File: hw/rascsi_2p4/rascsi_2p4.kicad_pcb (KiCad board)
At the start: 2 copper layers, 65 x 56 mm, 128 parts, among them J1 Raspberry_Pi_2_3, J10 Conn_01x04_Male, J2 DNP, J20 171826-4, J3 Conn_02x25_Odd_Even, J4 I2C Pinout, J5 DNP, J6 CONNFLY DB-25, J7 DNP, J8 USB_B_Micro, J9 Conn_02x25_Odd_Even, U1 74ALVC164245DGG, U2 74ALVC164245DGG, X1 Mac, X2 Dogcow, X3 Mac, X4 Dogcow, X5 Dogcow, X6 Dogcow, X7 Pi, X8 Pi

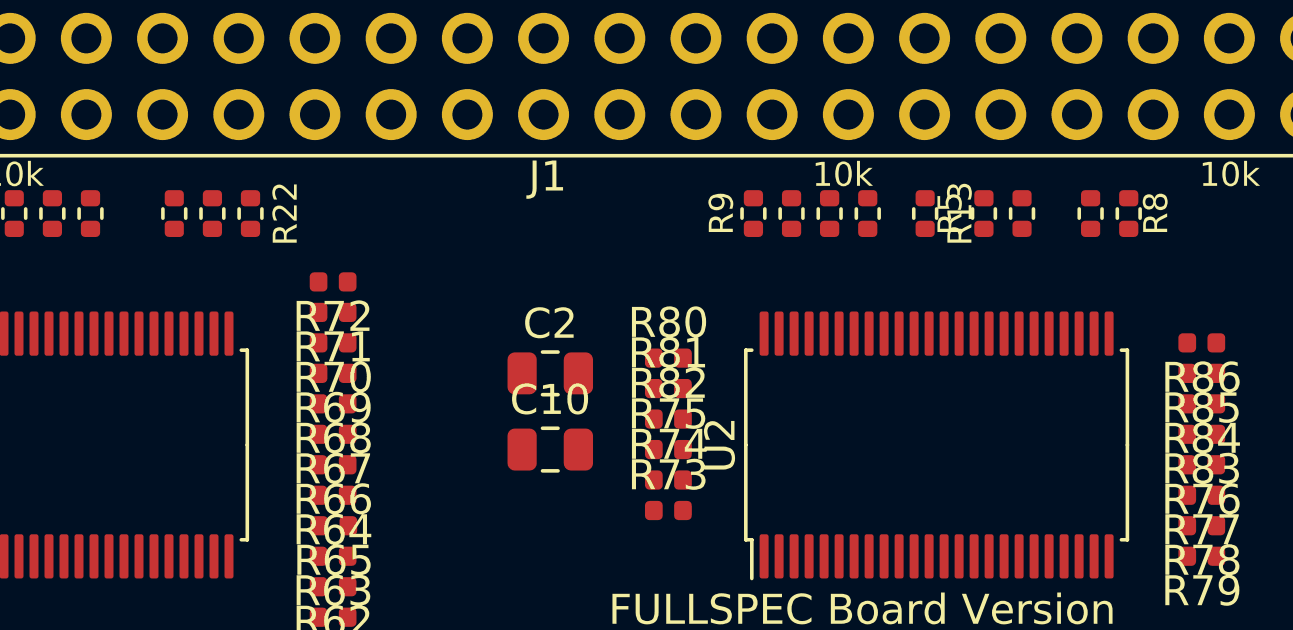
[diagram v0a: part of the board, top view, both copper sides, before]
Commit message: added intermediate routing results with 136 vias
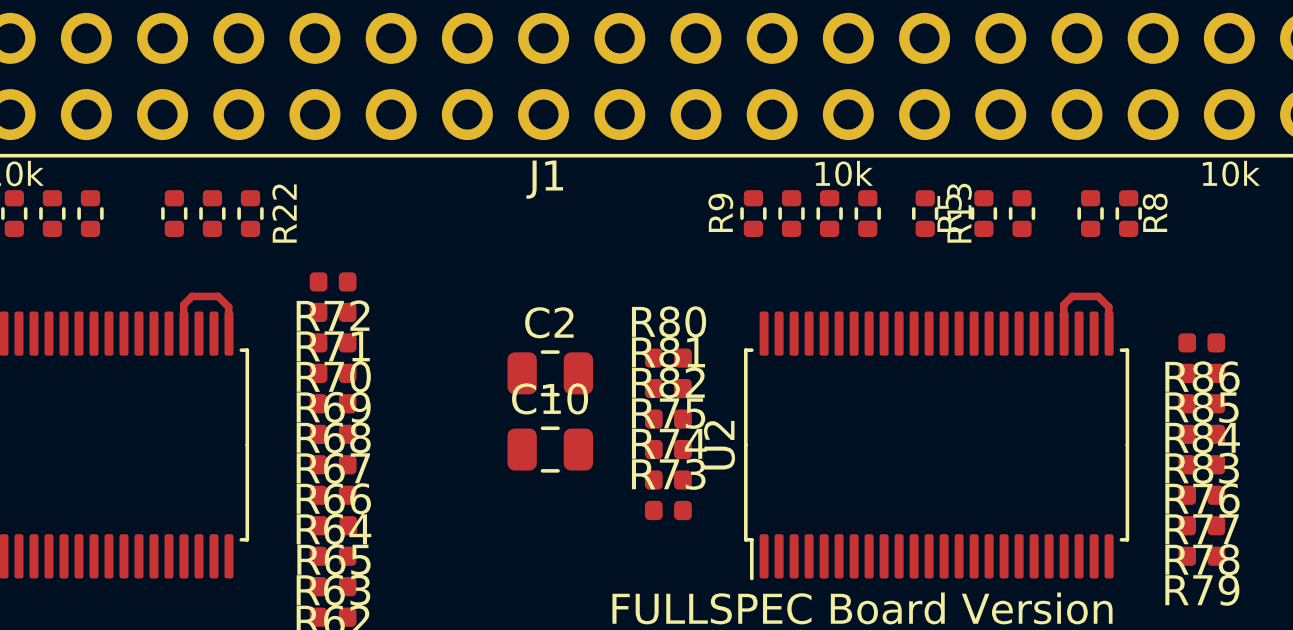
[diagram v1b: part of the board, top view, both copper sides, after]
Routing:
- net GND: track 0.00 -> 7.18 mm

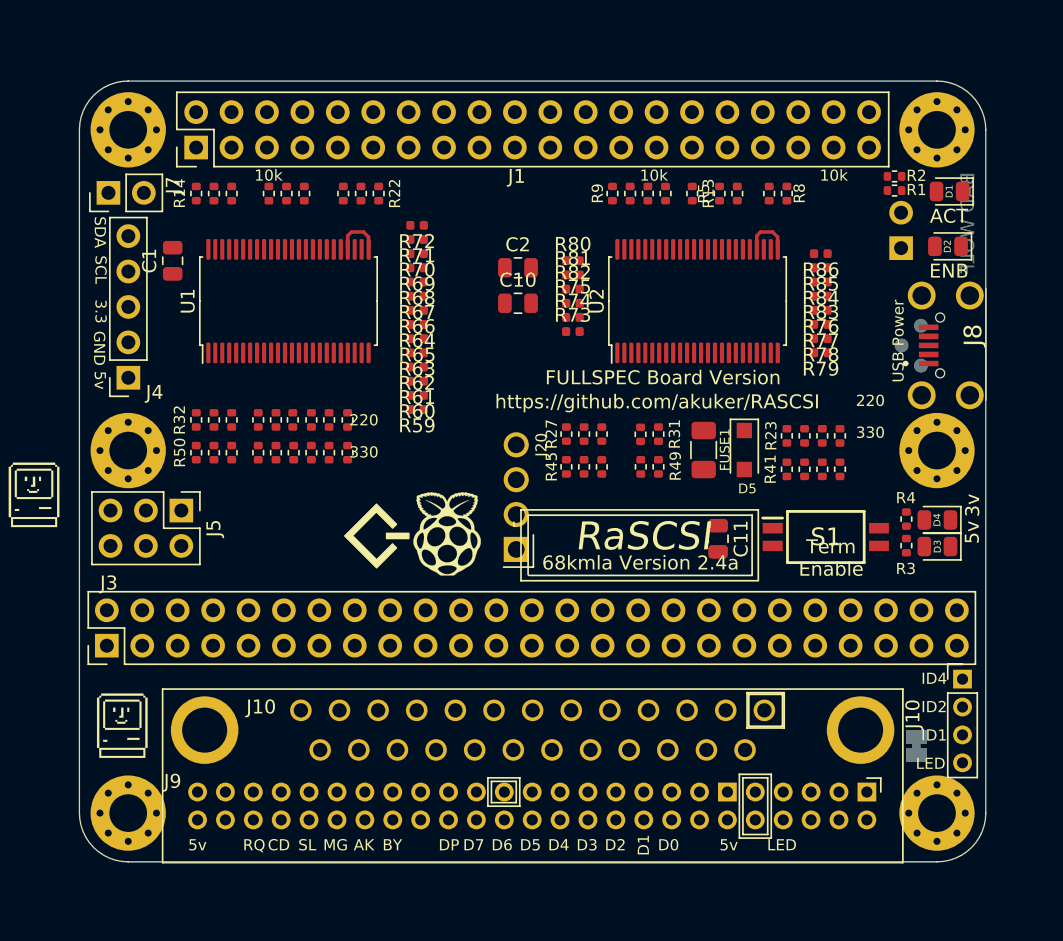
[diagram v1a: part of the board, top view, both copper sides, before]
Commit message: imported routed traces; fixed orientation of U1 and U2
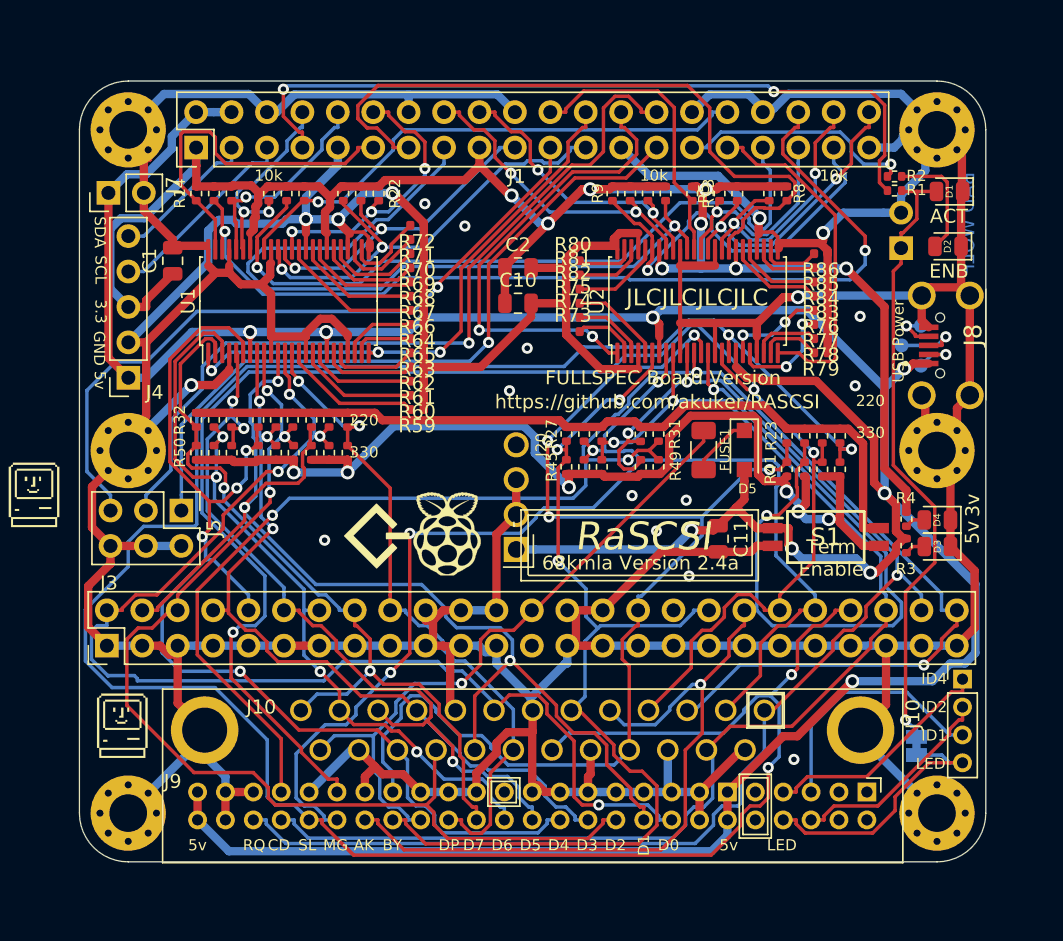
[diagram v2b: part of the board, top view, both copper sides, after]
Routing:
- net GND: track 7.18 -> 614.4 mm, vias 0 -> 19
- net +5V: track 0.00 -> 239.1 mm, vias 0 -> 9
- net C-SEL: track 0.00 -> 174.4 mm, vias 0 -> 4
- net +3V3: track 0.00 -> 133.7 mm, vias 0 -> 8
- net C-I_O: track 0.00 -> 119.3 mm, vias 0 -> 4
- net C-RST: track 0.00 -> 117.8 mm, vias 0 -> 3
- net C-ACK: track 0.00 -> 101.4 mm, vias 0 -> 3
- net C-REQ: track 0.00 -> 97.6 mm, vias 0 -> 3
- net C-MSG: track 0.00 -> 92.8 mm, vias 0 -> 4
- net C-C_D: track 0.00 -> 89.6 mm, vias 0 -> 2
- net C-ATN: track 0.00 -> 86.6 mm, vias 0 -> 4
- net C-D0: track 0.00 -> 86.0 mm, vias 0 -> 4
- net C-D1: track 0.00 -> 82.6 mm, vias 0 -> 3
- net C-D4: track 0.00 -> 80.6 mm, vias 0 -> 4
- net C-D2: track 0.00 -> 78.6 mm, vias 0 -> 3
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
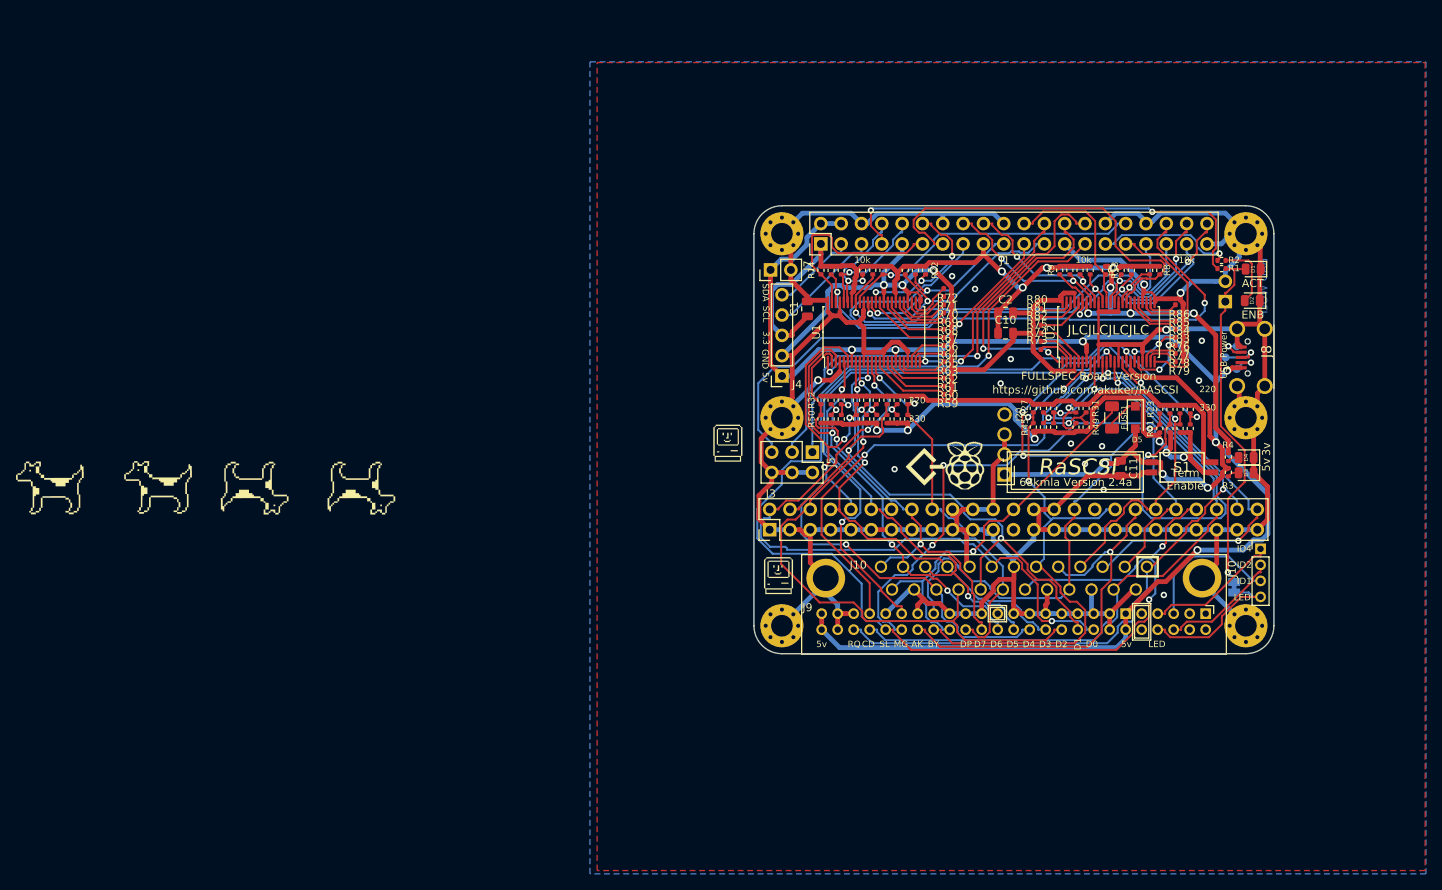
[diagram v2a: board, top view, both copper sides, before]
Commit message: added U1/U2 caps for 3.3V
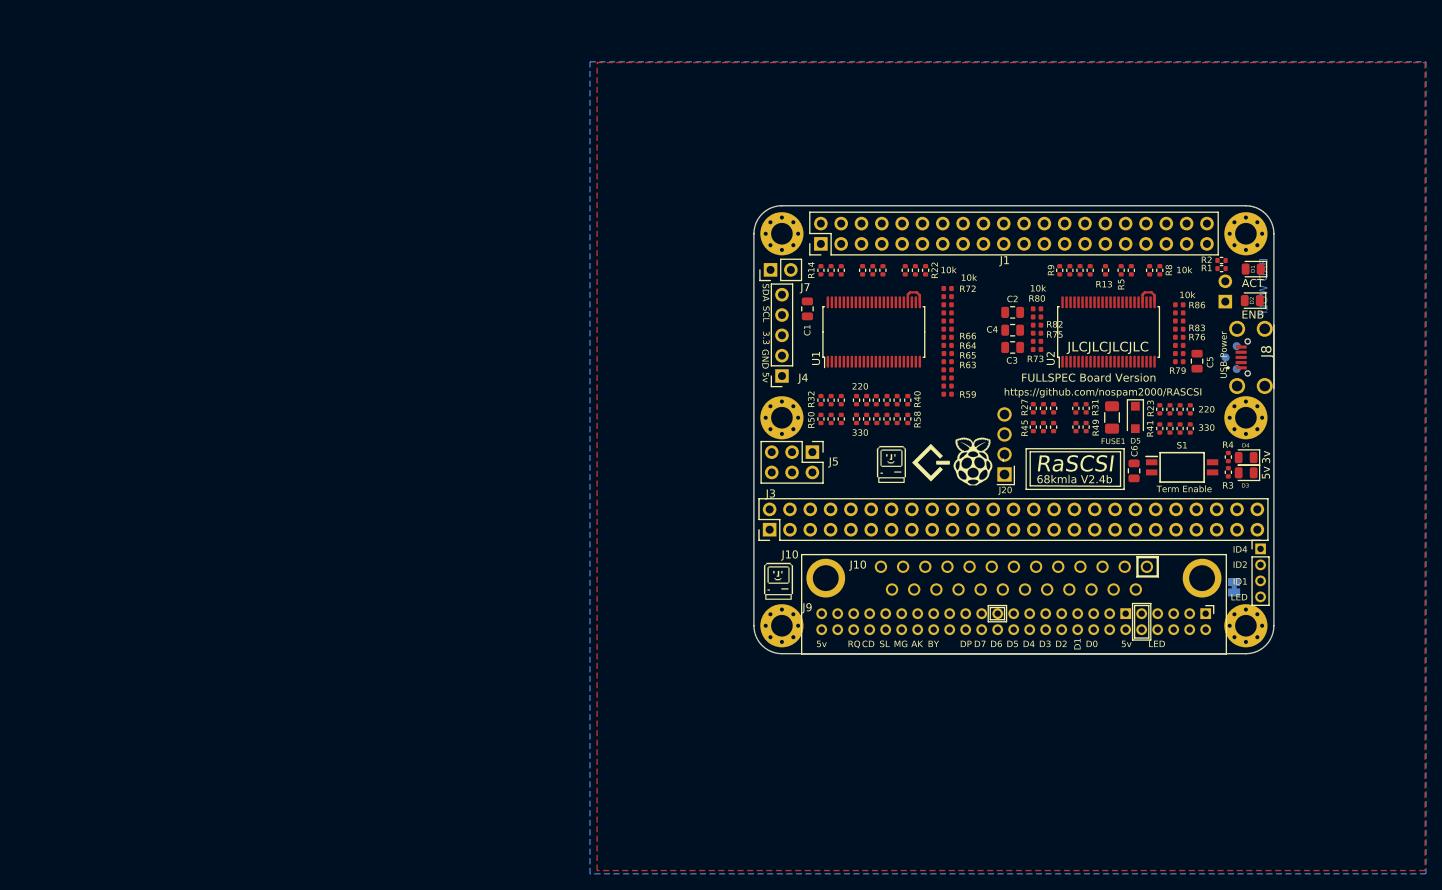
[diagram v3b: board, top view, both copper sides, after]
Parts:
- removed C11: 10u, Capacitor_SMD:C_0805_2012Metric
- removed X2, X4, X5, X6: Dogcow, SamacSys_Parts:dogcow
- added C4: 330n, Capacitor_SMD:C_0805_2012Metric, F.Cu at (206.8, 60.2)
- added C5: 330n, Capacitor_SMD:C_0805_2012Metric, F.Cu at (229.9, 61.9)
- added C6: 10u, Capacitor_SMD:C_0805_2012Metric, F.Cu at (222.0, 75.6)
- moved X3 20.6 mm to (191.7, 74.8)
- moved X7 1.14 mm to (201.9, 74.5)
- moved C3 0.97 mm to (206.8, 58.1)
- moved X8 0.96 mm to (196.5, 74.6)
- moved C2 0.89 mm to (206.8, 55.8)
- moved X1 0.71 mm to (177.6, 89.4)
- renumbered C10 to C3
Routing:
- net GND: track 614.4 -> 7.16 mm, vias 19 -> 0
- net +5V: track 239.1 -> 0.00 mm, vias 9 -> 0
- net C-SEL: track 174.4 -> 0.00 mm, vias 4 -> 0
- net +3V3: track 133.7 -> 0.00 mm, vias 8 -> 0
- net C-I_O: track 119.3 -> 0.00 mm, vias 4 -> 0
- net C-RST: track 117.8 -> 0.00 mm, vias 3 -> 0
- net C-ACK: track 101.4 -> 0.00 mm, vias 3 -> 0
- net C-REQ: track 97.6 -> 0.00 mm, vias 3 -> 0
- net C-MSG: track 92.8 -> 0.00 mm, vias 4 -> 0
- net C-C_D: track 89.6 -> 0.00 mm, vias 2 -> 0
- net C-ATN: track 86.6 -> 0.00 mm, vias 4 -> 0
- net C-D0: track 86.0 -> 0.00 mm, vias 4 -> 0
- net C-D1: track 82.6 -> 0.00 mm, vias 3 -> 0
- net C-D4: track 80.6 -> 0.00 mm, vias 4 -> 0
- net C-D2: track 78.6 -> 0.00 mm, vias 3 -> 0
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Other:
- board text added: "68kmla V2.4b"
- board text added: "https://github.com/nospam2000/RASCSI"
- board text removed: "https://github.com/akuker/RASCSI"
